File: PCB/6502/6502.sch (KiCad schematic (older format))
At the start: 1 part, among them U1 MOS_6502

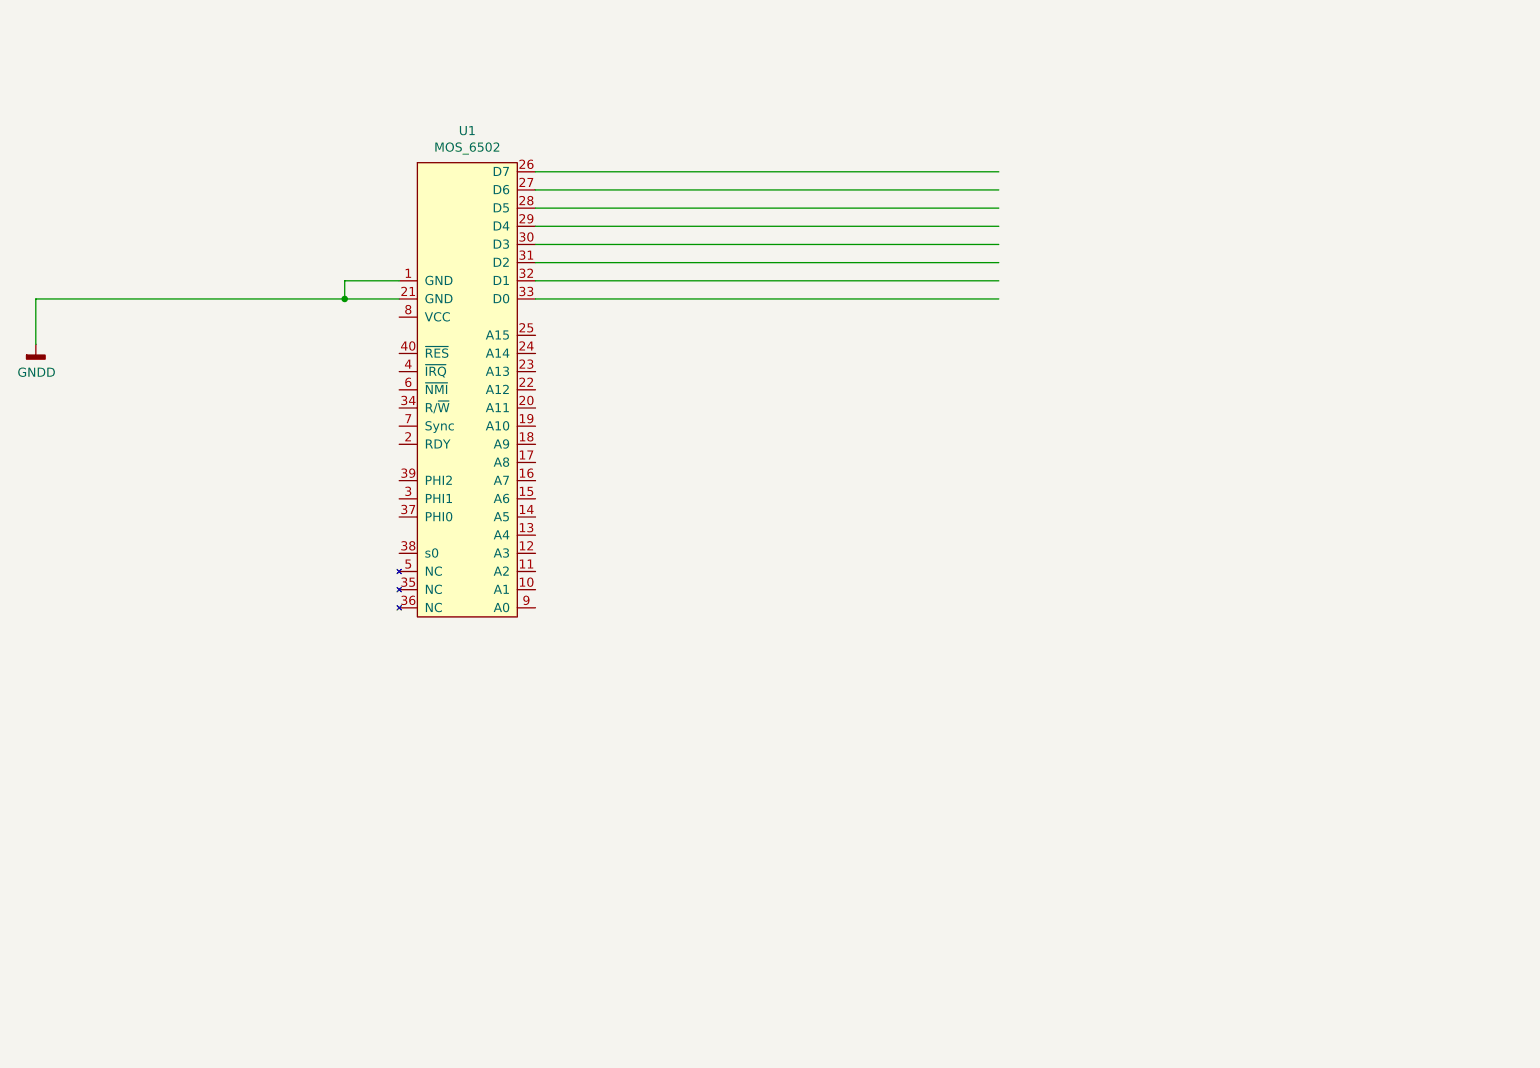
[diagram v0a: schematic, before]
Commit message: Added more PCB symbols
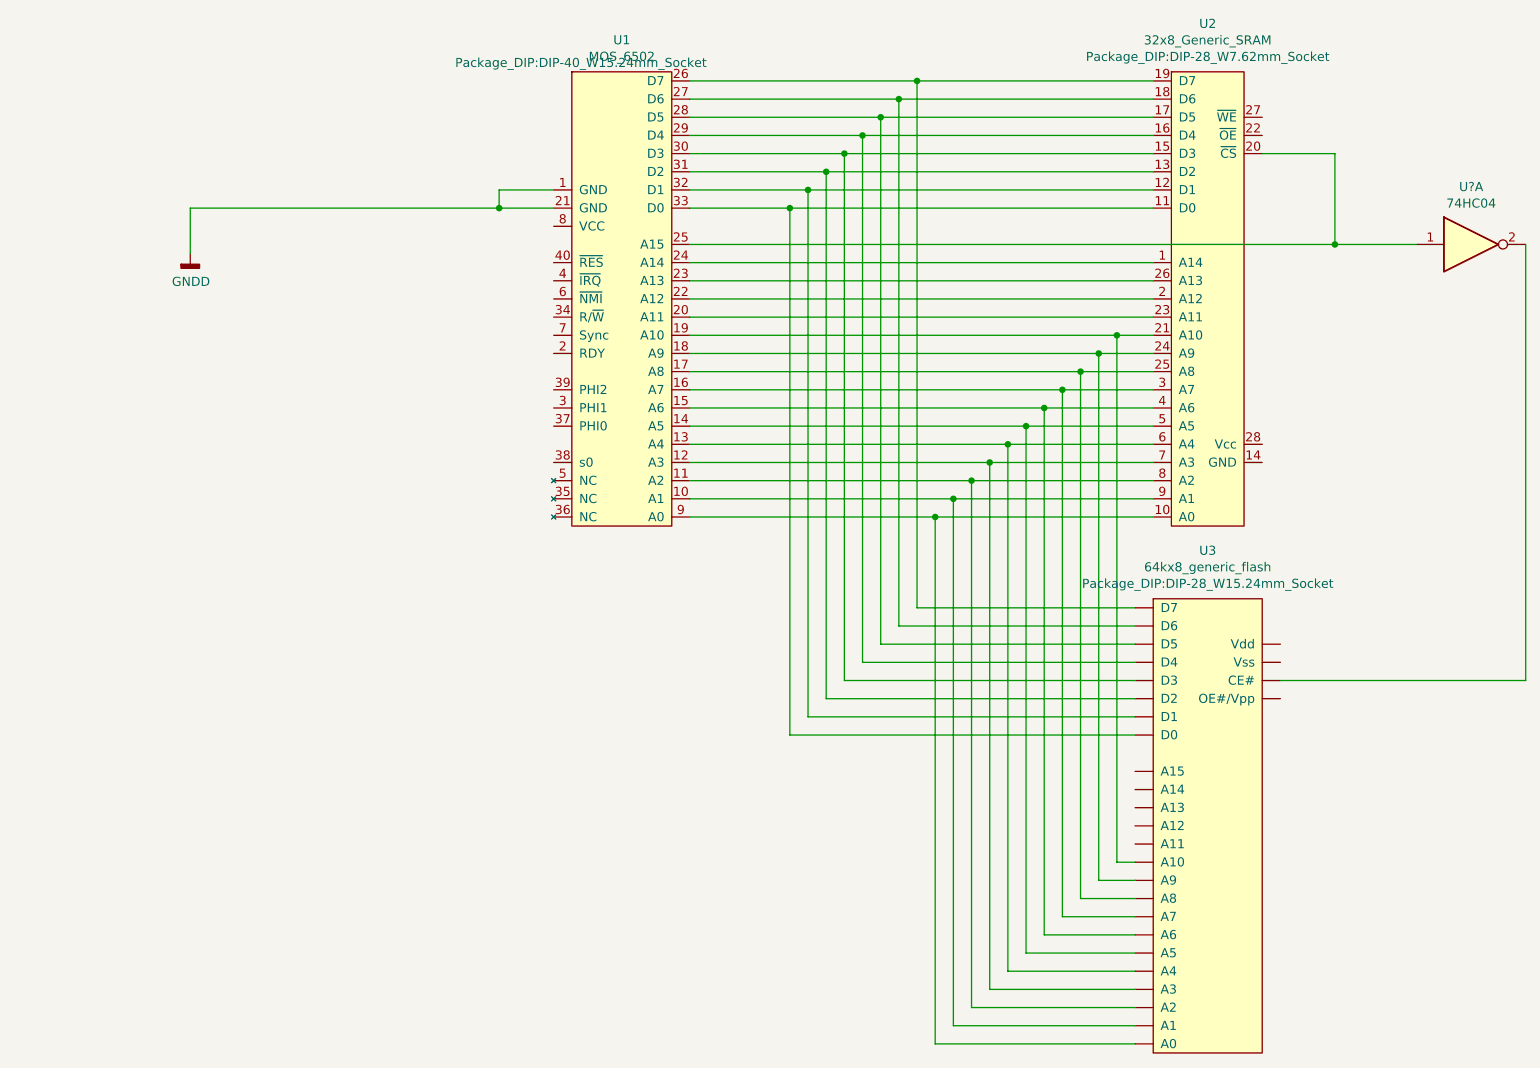
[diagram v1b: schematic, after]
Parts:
- added U2: 32x8_Generic_SRAM, Package_DIP:DIP-28_W7.62mm_Socket, symbol Memory_RAM:32x8_Generic_SRAM
- added U3: 64kx8_generic_flash, Package_DIP:DIP-28_W15.24mm_Socket, symbol Memory_RAM:64kx8_generic_flash
- added U?: 74HC04, symbol 74xx:74HC04
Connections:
- wire segments 13 -> 91
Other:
- moved on the sheet: U1
